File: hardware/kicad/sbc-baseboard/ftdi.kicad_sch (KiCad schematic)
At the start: 18 parts, among them J9 FTDI header, U501 FT231XS

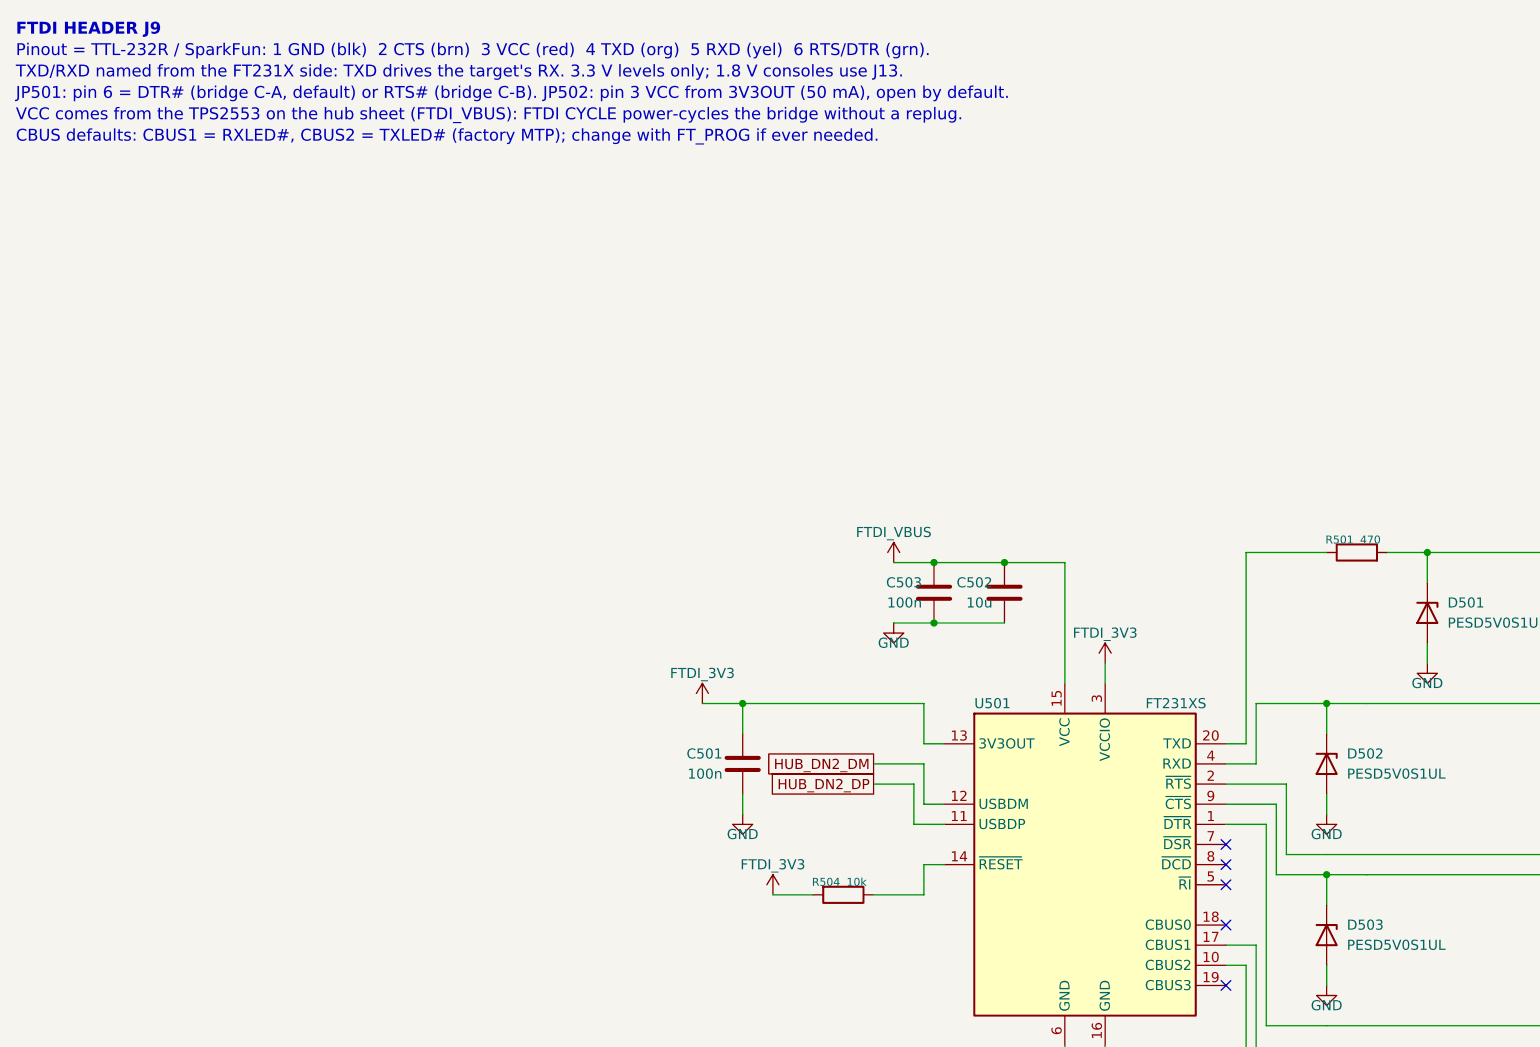
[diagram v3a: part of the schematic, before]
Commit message: Symbol name clearance, divider at the reading pin, inlet TVS orientation
Symbols: a top or bottom pin's name runs vertically into the body, so box
symbols now grow outward by whole rows wherever such a name would reach a
side pin's name (USB2517 three rows on top, K64 two rows top and bottom,
PCA9517A three rows on top); the side-pin rows stay where they were so the
sheet layouts are unaffected. U402's VDD names no longer print over USBUP_DP.

Frame pass: nothing on the sheet frame or the title block, enforced by the
layout gate (usable area 15..405 x 15..282 mm, title block from 300/253).

Flow pass: pull-ups hang up to their rail, pull-downs hang down (R408/R409
and the other strap and sense resistors). The J1 VBUS_DET divider sits at
U402 pin 44, the pin that reads it; J1's VBUS lane is a plain stretch that
U401 taps; J1 and U401 lifted clear of the hub's +3V3 bus. The hub's left
strap lanes turn in columns starting at x = 118.11 so they clear the bottom
decoupling ladders (fan() grew a turn_at argument for this).

Inlet TVS D102 hangs from J2's VBUS lane as a D_Zener with its cathode on
VBUS_IN. At 8579cd2 it was drawn with the bidirectional D_TVS symbol and
pad 1 (the SMA cathode) on GND, which would have forward-biased it.

Bucks: the FB pulls start past the catch diode's text; the two notes are
rewrapped and sit between U101 and the compensation parts.

Gates on every sheet: ERC 0, endpoint contacts 0, rail merges 0, frame 0,
no text on bodies or wires. Connectivity identical to 8579cd2 (symmetric
passives order-free) except the TVS orientation.

Co-Authored-By: Claude Fable 5.1 <noreply@anthropic.com>
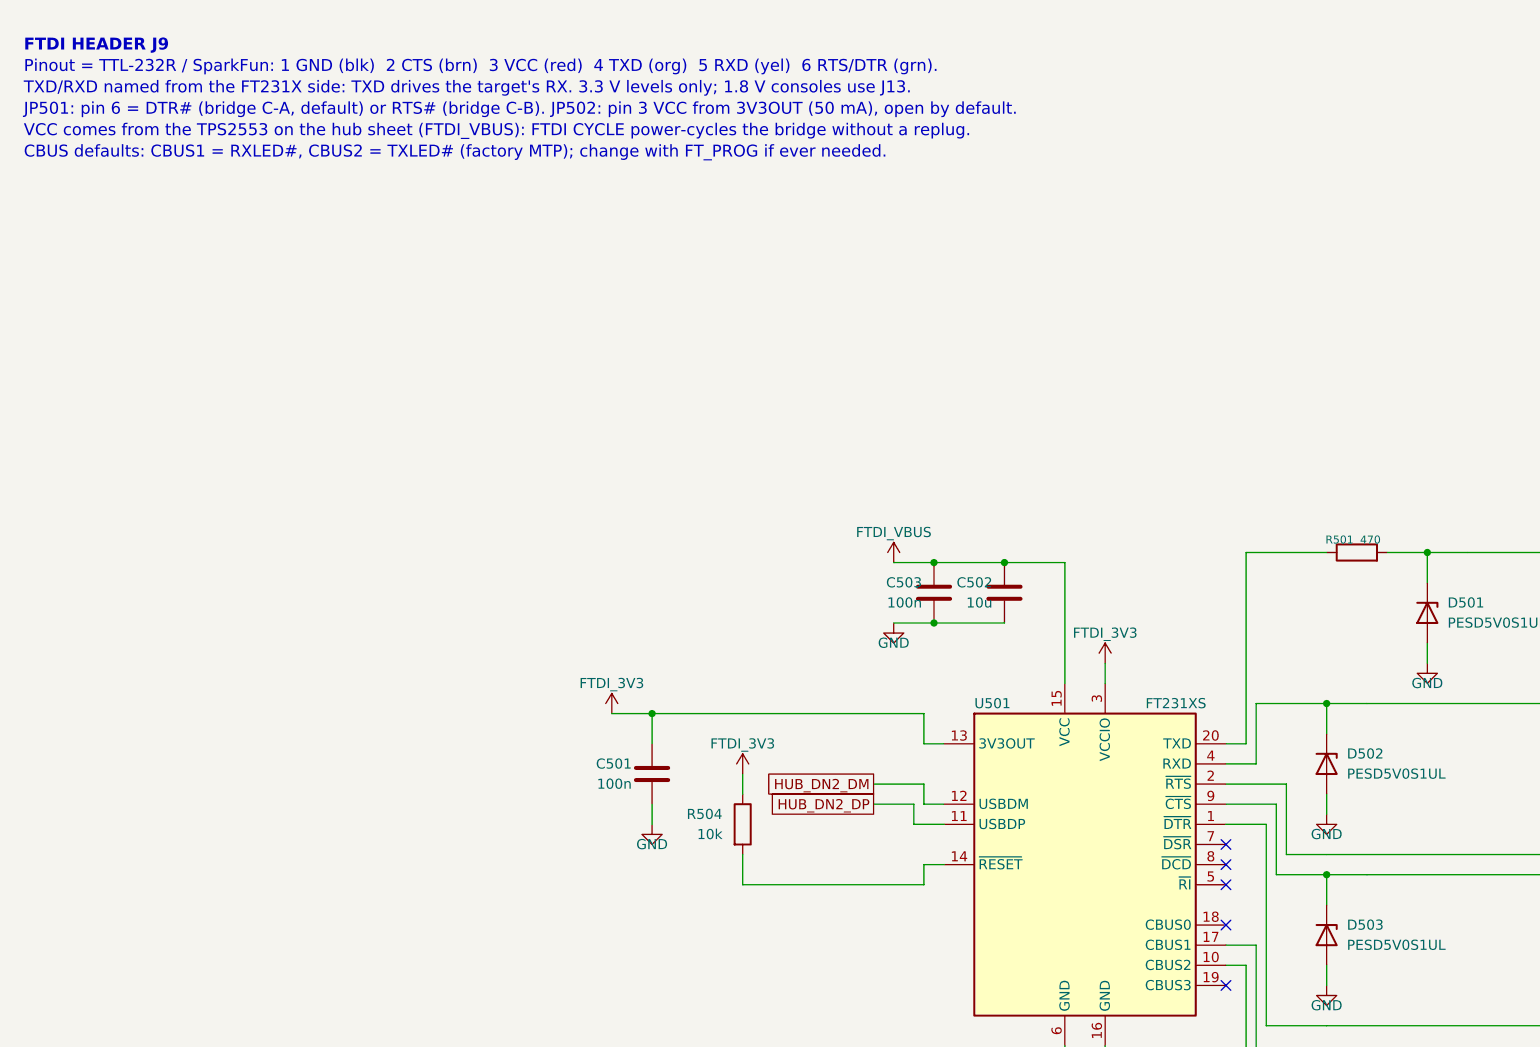
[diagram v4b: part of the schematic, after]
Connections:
- net FTDI_3V3: now also R504.1; no longer R504.2
- net at U501.14 (~{RESET}): now also R504.2; no longer R504.1

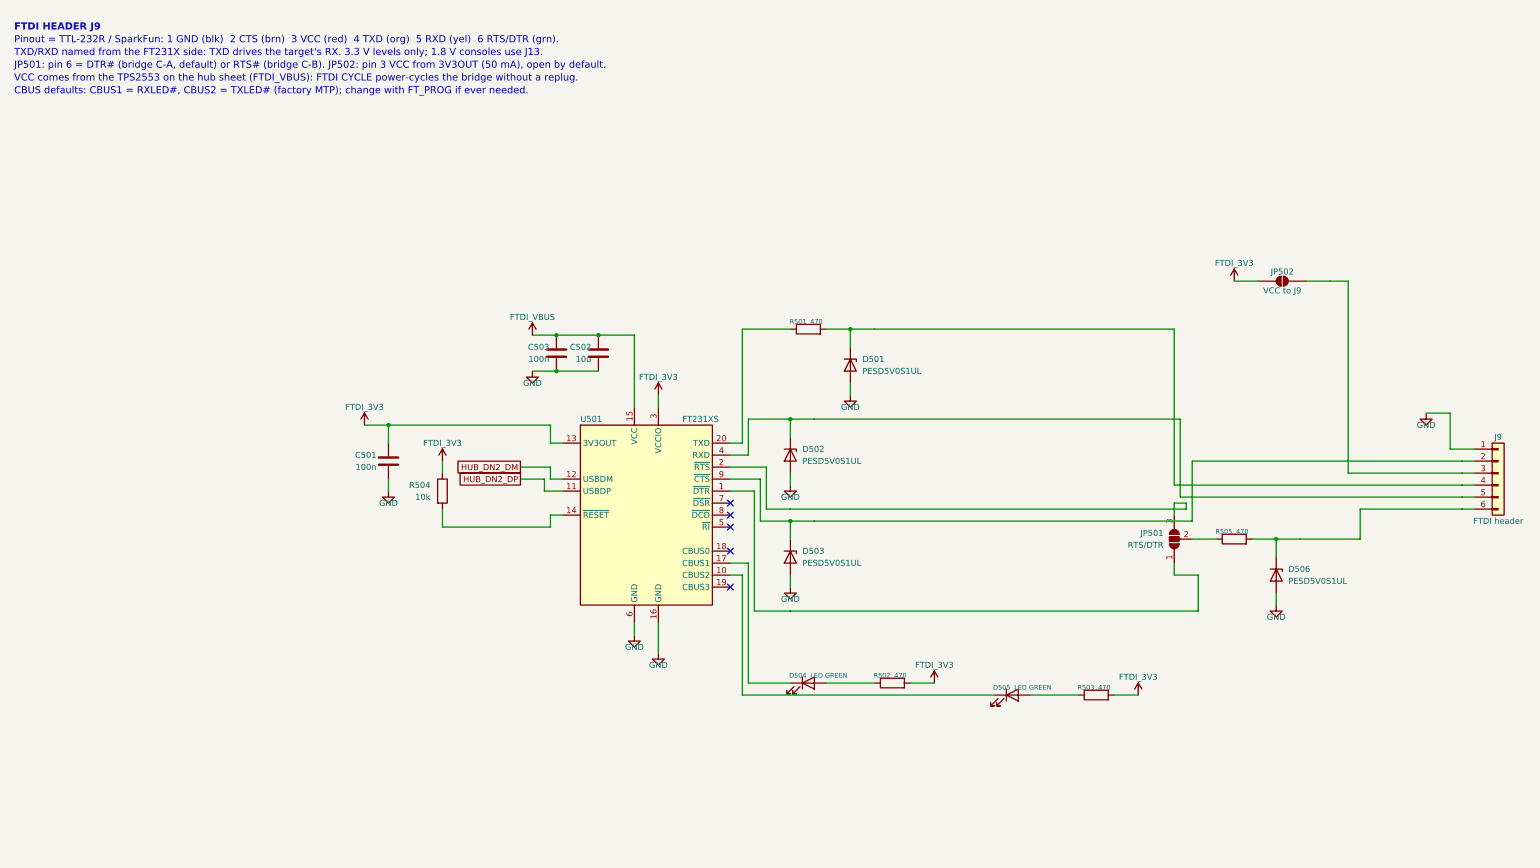
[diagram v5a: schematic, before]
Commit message: Reference-design review; pin numbers and real text widths in the layout gate
Review (docs/reference-design-review.md): every IC's surrounding parts
compared with its datasheet typical application or evaluation board.
Brought in line:
- TPS54560B compensation 16.9k / 4.7 nF / 47 pF (the 5 V / 400 kHz design
  example, same 141 uF ceramic output); the placeholders are gone.
- TPS62823 divider 453k / 100k with the 120 pF feed-forward capacitor the
  datasheet recommends.
- USB2517 VBUS_DET from the EVB: 100k / 100k with 1 uF (was 10k / 22k, 3.4 V
  at a 3.3 V pin).
- KSZ8081 MDIO pull-up 1.0k as the datasheet requires (was 4.7k).
- FT231X: 27 R in series and 47 pF on USBDM/USBDP, datasheet figure 6.1.
Deviations kept and documented: the bucks' EN gated by the PD controller
instead of a UVLO divider, the FT231X fed by a power switch instead of a
ferrite bead, translator OE tied to the target rail.

Layout gate: pin numbers are text boxes like any other, and all text widths
come from a per-glyph table fitted to the extents KiCad writes into its PDF
(check_pins.py); the generator's spacing uses the same table. That exposed
and fixed: reference/value overlaps on narrow symbols (now stacked), rail
names printed over each other (the lane end and hanging pull-up now carry
half the rail name), a port-switch value over its pin number, turned parts
with text on the pin side, lane stacks whose spread collapsed at the grid
snap, routes landing on connector pin stubs (J16, J601, J14, D202 moved),
the PD controller's I2C and gate routes that crossed half the sheet (now
labels), and the port /FAULT and I2C1 pull-ups, which as hanging resistors
staggered off the sheet and are now one column to one +3V3 symbol. The
port switch carries FAULT above OUT so the switched rail's parts hang below
the label; the VBUS row is drawn from the connector back to the switch.

All sheets: ERC 0, contacts 0, merges 0, layout 0 in every category.
Connectivity against 8579cd2 differs only in the value ch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
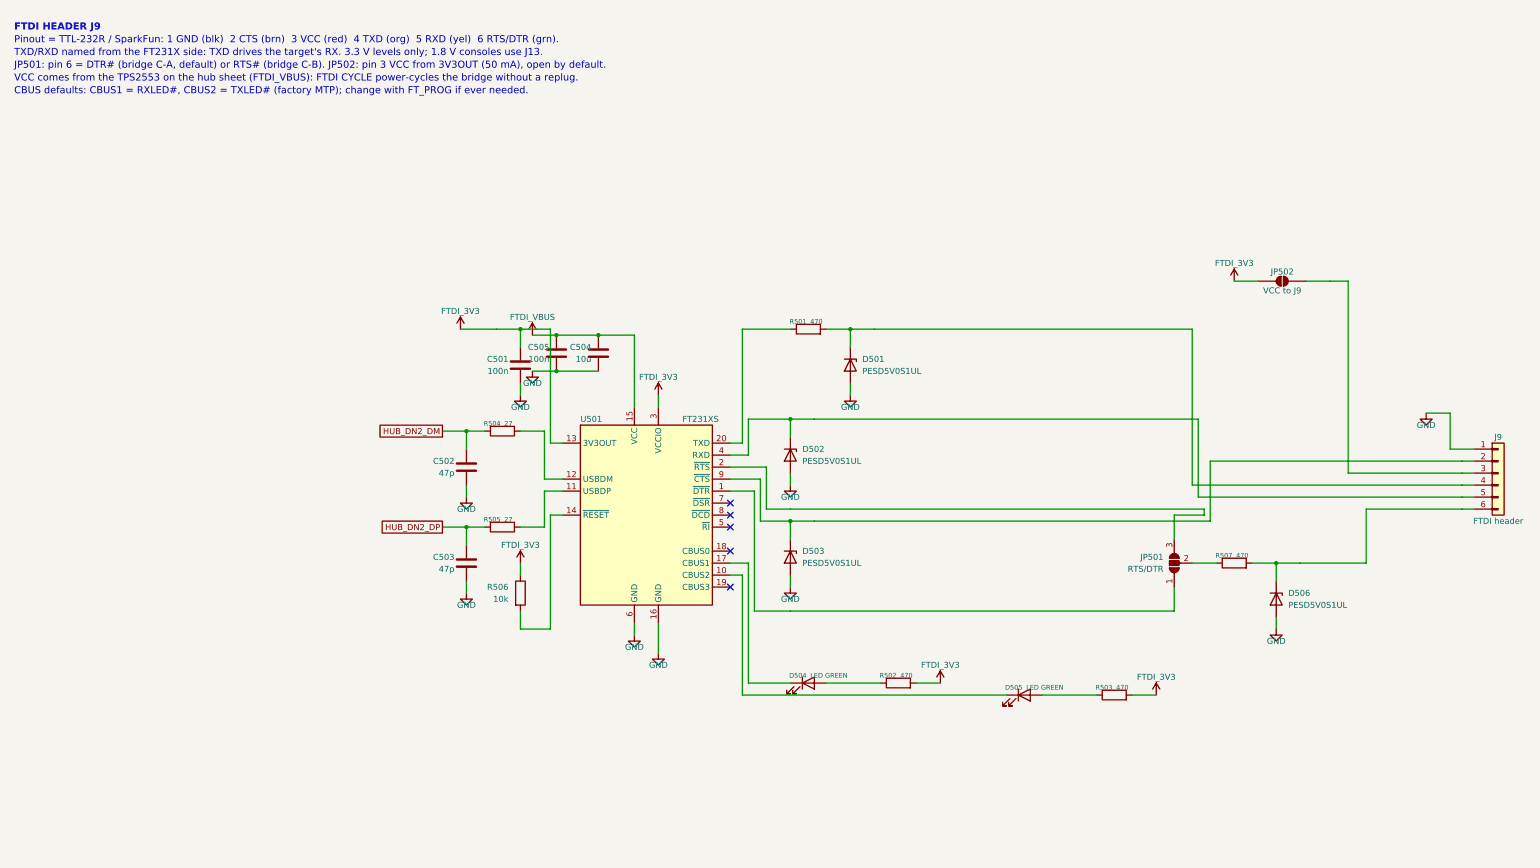
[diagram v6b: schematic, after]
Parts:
- added C504: 10u, Capacitor_SMD:C_0805_2012Metric, symbol Device:C
- added C505: 100n, Capacitor_SMD:C_0603_1608Metric, symbol Device:C
- added R506: 10k, Resistor_SMD:R_0603_1608Metric, symbol Device:R
- added R507: 470, Resistor_SMD:R_0603_1608Metric, symbol Device:R
- C502: value 10u -> 47p; footprint Capacitor_SMD:C_0805_2012Metric -> Capacitor_SMD:C_0603_1608Metric
- C503: value 100n -> 47p
- R504: value 10k -> 27
- R505: value 470 -> 27
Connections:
- net FTDI_3V3: now also R506.1; no longer R504.1
- net FTDI_VBUS: now also C504.1, C505.1; no longer C502.1, C503.1
- net GND: now also C504.2, C505.2
- net HUB_DN2_DM: now also C502.1, R504.2; no longer U501.12 (USBDM)
- net HUB_DN2_DP: now also C503.1, R505.2; no longer U501.11 (USBDP)
- net at D506.1 (K), J9.6 (Pin_6): now also R507.2; no longer R505.2
- net at U501.14 (~{RESET}): now also R506.2; no longer R504.2
- net at JP501.2 (C): now also R507.1; no longer R505.1
- new net: R504.1, U501.12 (USBDM)
- new net: R505.1, U501.11 (USBDP)
